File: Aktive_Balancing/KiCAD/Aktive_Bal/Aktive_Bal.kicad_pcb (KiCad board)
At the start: 4 copper layers, 108.8 x 101.3 mm, 219 parts, among them J1 Screw_Terminal_01x02, J10 Conn_01x02_Pin, J11 Conn_01x02_Pin, J12 Conn_01x02_Pin, J13 Conn_01x02_Pin, J14 Conn_01x02_Pin, J15 Screw_Terminal_01x03, J16 Screw_Terminal_01x03, J17 Screw_Terminal_01x03, J18 Screw_Terminal_01x03, J19 Screw_Terminal_01x03, J2 A-DF_09_A_KG-T4S, J20 Screw_Terminal_01x03, J21 Conn_01x02_Pin, J22 Conn_01x02_Pin, J23 Conn_01x02_Pin, J24 Conn_01x02_Pin, J3 Conn_01x02_Pin, J4 Conn_01x02_Pin, J5 Conn_01x02_Pin, J6 Conn_01x02_Pin, J7 Sockel_BluePill, J9 Conn_01x02_Pin, Q1 BSS316NH6327XTSA1, Q10_H1 NTTFS6H888NL, Q10_L1 NTTFS6H888NL, Q11_H1 NTTFS6H888NL, Q11_L1 NTTFS6H888NL, Q12_H1 NTTFS6H888NL, Q12_L1 NTTFS6H888NL, Q13_H1 NTTFS6H888NL, Q13_L1 NTTFS6H888NL, Q14_H1 NTTFS6H888NL, Q14_L1 NTTFS6H888NL, Q15_H1 NTTFS6H888NL, Q15_L1 NTTFS6H888NL, Q16_H1 NTTFS6H888NL, Q16_L1 NTTFS6H888NL, Q1_H1 NTTFS6H888NL, Q1_L1 NTTFS6H888NL, Q2_H1 NTTFS6H888NL, Q2_L1 NTTFS6H888NL, Q3_H1 NTTFS6H888NL, Q3_L1 NTTFS6H888NL, Q4_H1 NTTFS6H888NL, Q4_L1 NTTFS6H888NL, Q5_H1 NTTFS6H888NL, Q5_L1 NTTFS6H888NL, Q6_H1 NTTFS6H888NL, Q6_L1 NTTFS6H888NL, Q7_H1 NTTFS6H888NL, Q7_L1 NTTFS6H888NL, Q8_H1 NTTFS6H888NL, Q8_L1 NTTFS6H888NL, Q9_H1 NTTFS6H888NL, Q9_L1 NTTFS6H888NL, U1 RFP12N10L, U10 LTV-847S, U11 LTV-847S, U12 LTV-847S, U13 LTV-847S, U14 TL084, U15 LM2596S-ADJ, U2 ADUM1250ARZ-RL7, U3 SN65HVD233, U4 SCW20C-12, U5 EC1SA16N, U6 PCA9306DC, U7 PCF8575CDB, U8 LM1117MP-3.3, U9 MCP4725xxx-xCH

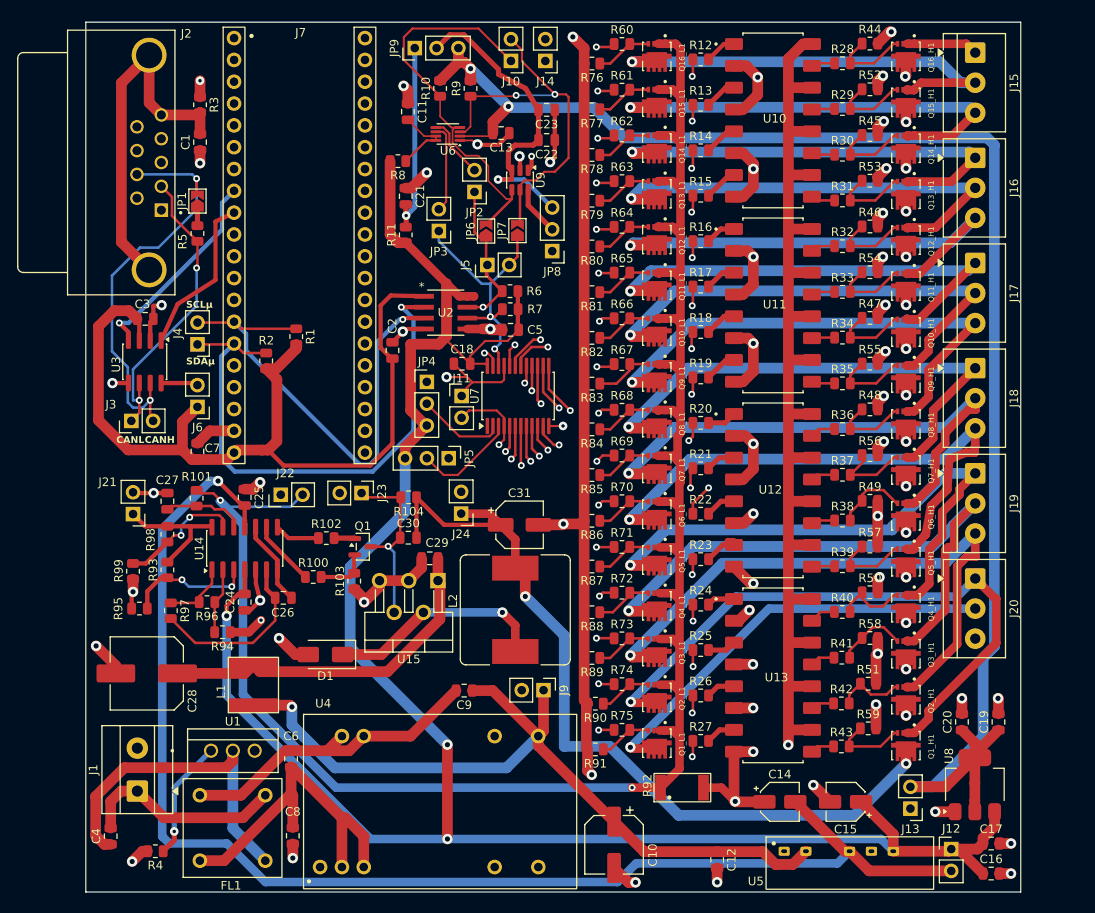
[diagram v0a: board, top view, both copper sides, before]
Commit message: Layout fürs erste fertig gemacht
Erste vollständig geroutete Version; Silkscreens sind auch halbwegs gut
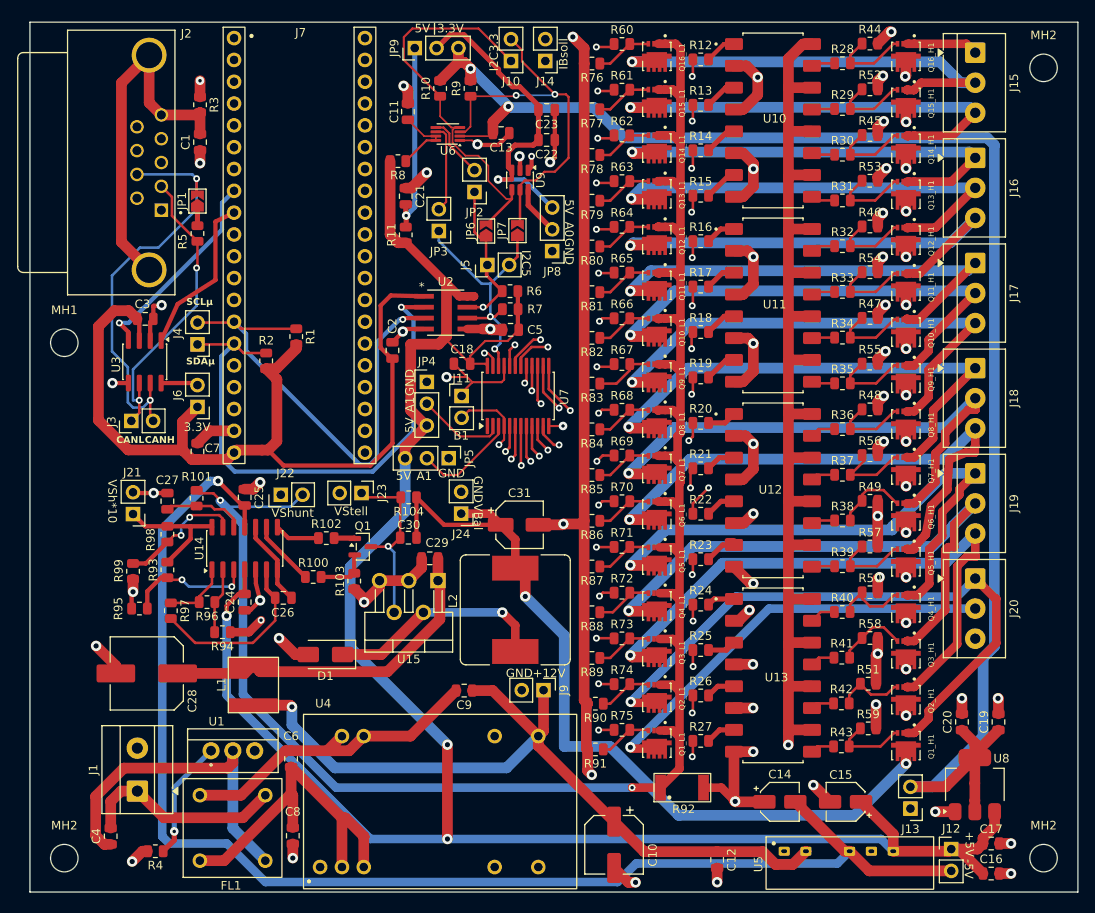
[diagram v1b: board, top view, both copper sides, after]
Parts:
- added MH1: MountingHole_3.2mm_M3_ISO7380, MountingHole:MountingHole_3.2mm_M3_ISO7380, F.Cu at (125.0, 56.3)
- added MH2: MountingHole_3.2mm_M3_ISO7380, MountingHole:MountingHole_3.2mm_M3_ISO7380, F.Cu at (125.0, 116.3)
- added MH2: MountingHole_3.2mm_M3_ISO7380, MountingHole:MountingHole_3.2mm_M3_ISO7380, F.Cu at (239.0, 116.3)
- added MH2: MountingHole_3.2mm_M3_ISO7380, MountingHole:MountingHole_3.2mm_M3_ISO7380, F.Cu at (239.0, 24.3)
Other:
- board size 108.8 x 101.3 mm -> 122 x 101.3 mm
- board text added: "+12V"
- board text added: "+5V"
- board text added: "-5V"
- board text added: "3.3V"
- board text added: "5V"
- board text added: "A0"
- board text added: "A1"
- board text added: "B1"
- board text added: "GND"
- board text added: "I2C3.3"
- board text added: "I2C5"
- board text added: "IBsoll"
- board text added: "VBal"
- board text added: "VSh*10"
- board text added: "VShunt"
- board text added: "VStell"

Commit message: quetschen
brücken getauscht
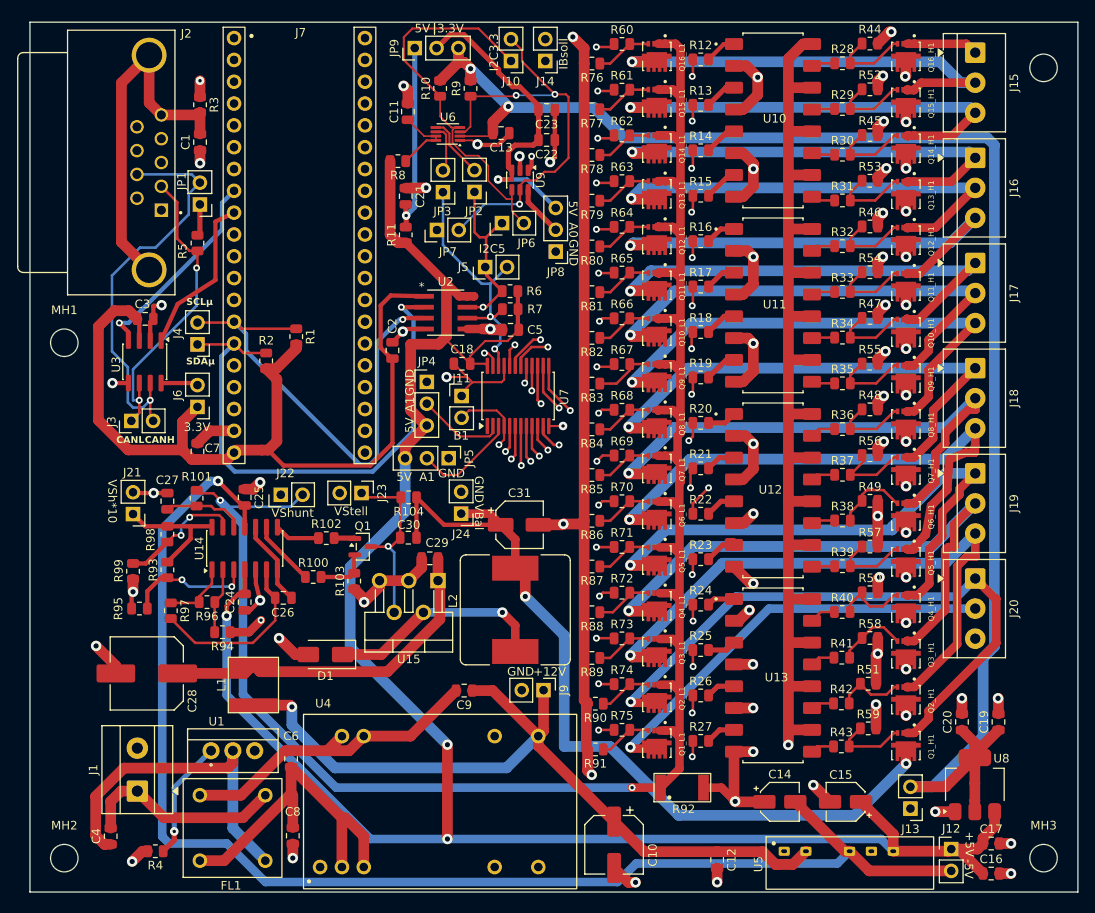
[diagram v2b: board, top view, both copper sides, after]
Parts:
- JP1, JP6, JP7: footprint Jumper:SolderJumper-2_P1.3mm_Open_TrianglePad1.0x1.5mm -> Connector_PinHeader_2.54mm:PinHeader_1x02_P2.54mm_Vertical
- moved JP7 9.37 mm to (168.4, 43.2)
- moved JP3 4.55 mm to (169.1, 38.8)
- moved JP6 2.07 mm to (176.0, 42.4)
- moved R5 1.12 mm to (140.5, 44.7)
- moved JP1 0.49 mm to (140.8, 40.2), turned to 180 degrees
- moved JP8 0.41 mm to (182.2, 45.7)
- moved J5 0.35 mm to (174.0, 47.5)
- renumbered MH2 to MH3, MH2 to MH4
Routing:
- net SCL3.3: track 43.9 -> 49.8 mm, vias 2 -> 3
- net Net-(JP3-B): track 10.4 -> 5.64 mm
- net SDA5: track 29.7 -> 32.1 mm
- net CANH: track 49.0 -> 47.1 mm, vias 2 -> 1
- net Net-(JP1-A): track 2.14 -> 3.71 mm
- net I_Bal_Soll: track 87.3 -> 88.2 mm
- net SDA3.3: track 46.7 -> 45.8 mm
- net GND_float2: track 298.4 -> 297.6 mm
- net Net-(JP8-B): track 36.8 -> 37.6 mm
- net Net-(JP8-C): track 5.76 -> 6.34 mm
- net CANL: track 35.3 -> 35.8 mm

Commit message: bisschen abstände und so
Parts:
- moved C4 13.0 mm to (136.2, 102.1), turned to 180 degrees
- moved J1 3.07 mm to (131.9, 111.1)
- moved C9 2.66 mm to (168.9, 97.0)
- moved FL1 1.09 mm to (147.3, 116.7)
- moved U1 1.09 mm to (141.0, 103.9)
- moved R4 1.09 mm to (134.5, 115.6)
- moved MH2 0.85 mm to (124.4, 116.9)
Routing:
- net Net-(U1-D): track 40.1 -> 21.9 mm
- net BAT+: track 24.0 -> 35.9 mm
- net +12V: track 232.0 -> 234.6 mm
- net Net-(C6-Pad2): track 37.3 -> 35.7 mm
- net SDAµC: track 65.2 -> 65.8 mm
- net enable: track 73.9 -> 74.5 mm
- net GNDµ: track 24.1 -> 23.9 mm, vias 5 -> 6

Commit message: Kleine Änderung canbus
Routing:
- net CANH: track 47.1 -> 44.0 mm
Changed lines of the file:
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@@
 	)
 	(segment
-		(start 130.55 57.301472)
-		(end 132.4 59.151472)
+		(start 134.15 63.85)
+		(end 135 63)
 		(width 0.3)
 		(layer "B.Cu")
@@
 	)
 	(segment
-		(start 130.55 48.494586)
-		(end 130.55 57.301472)
-		(width 0.3)
-		(layer "B.Cu")
-		(net "CANH")
-	)
-	(segment
-		(start 132.4 59.151472)
+		(start 132.4 56.202082)
 		(end 132.4 63.248528)
-		(width 0.3)
-		(layer "B.Cu")
-		(net "CANH")
-	)
-	(segment
-		(start 135.62 45.237)
-		(end 139.486972 41.370028)
 		(width 0.3)
 		(layer "B.Cu")
@@
 	)
 	(segment
-		(start 134.15 63.85)
-		(end 135 63)
-		(width 0.3)
-		(layer "B.Cu")
-		(net "CANH")
-	)
-	(segment
-		(start 139.486972 41.370028)
-		(end 139.486972 38.963866)
-		(width 0.3)
-		(layer "B.Cu")
-		(net "CANH")
-	)
-	(segment
-		(start 139.486972 38.963866)
-		(end 140.786972 37.663866)
+		(start 133.4575 36.71)
+		(end 130.55 39.6175)
 		(width 0.3)
 		(layer "B.Cu")
@@
 	)
 	(segment
+		(start 133.001472 63.85)
+		(end 134.15 63.85)
+		(width 0.3)
+		(layer "B.Cu")
+		(net "CANH")
+	)
+	(segment
+		(start 130.55 54.352082)
+		(end 132.4 56.202082)
+		(width 0.3)
+		(layer "B.Cu")
+		(net "CANH")
+	)
+	(segment
 		(start 139.833106 36.71)
 		(end 133.4575 36.71)
@@
 	)
 	(segment
-		(start 135.62 45.237)
-		(end 133.807586 45.237)
+		(start 130.55 39.6175)
+		(end 130.55 54.352082)
 		(width 0.3)
 		(layer "B.Cu")
-		(net "CANH")
-	)
-	(segment
-		(start 133.001472 63.85)
-		(end 134.15 63.85)
-		(width 0.3)
-		(layer "B.Cu")
-		(net "CANH")
-	)
-	(segment
-		(start 133.807586 45.237)
-		(end 130.55 48.494586)
-		(width 0.3)
-		(layer "B.Cu")

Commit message: review
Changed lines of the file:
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@@
-	)
-	(segment
-		(start 199.412 108.099)
-		(end 201.499 108.099)
-		(width 1)
-		(layer "F.Cu")
-		(net "GND_float2")
 	)
 	(segment
@@
 	)
 	(segment
-		(start 201.499 108.099)
-		(end 203.1 109.7)
-		(width 1)
-		(layer "F.Cu")
-		(net "GND_float2")
-	)
-	(segment
 		(start 219.699163 76.475837)
 		(end 219.7 76.475)
@@
 	)
 	(segment
+		(start 201.499 108.099)
+		(end 203.1 109.7)
+		(width 1.25)
+		(layer "F.Cu")
+		(net "GND_float2")
+	)
+	(segment
 		(start 205.216 71.009171)
 		(end 205.216 68.072)
@@
 		(width 1.25)
 		(layer "F.Cu")
+		(net "GND_float2")
+	)
+	(segment
+		(start 199.412 108.099)
+		(end 201.499 108.099)
+		(width 1.25)
+		(layer "F.Cu")

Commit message: Vorläufige finale Version
Diese Version soll in die Fertigung gehen.
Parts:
- added R200: 10k, Resistor_SMD:R_0805_2012Metric, F.Cu at (138.2, 77.4)
- added R201: 100k, Resistor_SMD:R_0805_2012Metric, F.Cu at (130.8, 79.6)
- added R202: 0, Resistor_SMD:R_0805_2012Metric, F.Cu at (200.9, 111.5)
- R98: value 90k -> 100k
- moved R98 3.52 mm to (133.5, 79.0), turned to 90 degrees
- moved J21 2.34 mm to (133.2, 73.9), turned to -90 degrees
- moved C27 1.03 mm to (136.1, 74.3)
- moved R101 0.86 mm to (139.5, 74.3)
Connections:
- C27 pad 2: Net-(U14D-+) -> Net-(C27-Pad2)
- J21 pad 1: I_Bal -> GND_float2
- J21 pad 2: GND_float2 -> I_Bal
- R101 pad 1: Net-(U14D-+) -> Net-(C27-Pad2)
- R92 pad 2: GND_float2 -> V_Shunt_Low
- R99 pad 2: GND_float2 -> V_Shunt_Low
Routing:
- net V_Shunt_Low: track 0.00 -> 114.7 mm, vias 0 -> 2
- net Net-(U14D-+): track 10.5 -> 19.0 mm
- net I_Bal: track 15.1 -> 21.8 mm, vias 0 -> 1
- net Net-(C27-Pad2): track 0.00 -> 6.12 mm
- net GND_float2: track 297.5 -> 294.3 mm
- net Net-(U14D--): track 14.6 -> 17.2 mm, vias 2 -> 0
- net V_I_Bal: track 223.7 -> 224.6 mm
- net TX: track 19.1 -> 18.4 mm
